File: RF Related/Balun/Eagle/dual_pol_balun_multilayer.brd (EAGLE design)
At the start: 54.6 x 48.6 mm, 8 parts, among them T1 ADT1-1WT+, T2 ADT1-1WT+, X1 SMA-142-0701-801/806, X2 SMA-142-0701-801/806, X3 SMA-142-0701-801/806, X4 SMA-142-0701-801/806, X5 SMA-142-0701-801/806, X6 SMA-142-0701-801/806

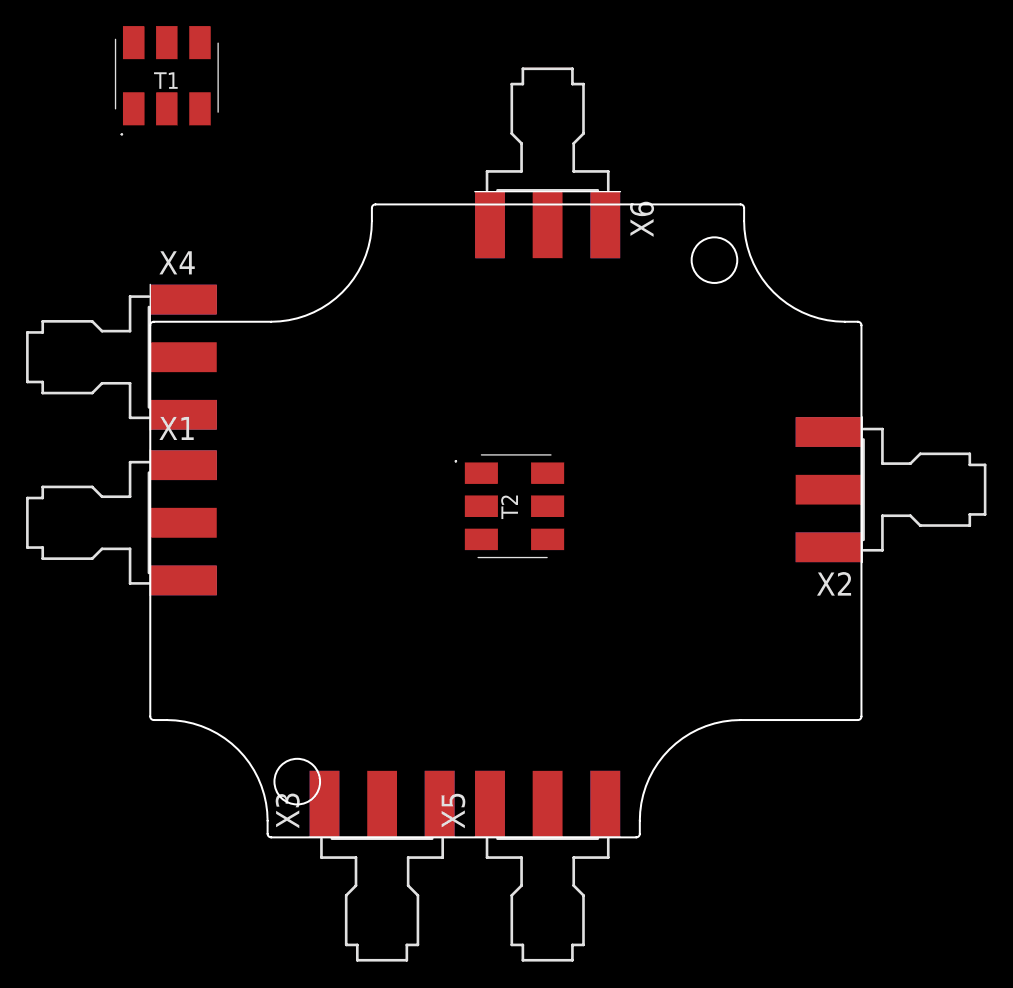
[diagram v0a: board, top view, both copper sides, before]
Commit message: also updated entire drone 3D model to contain primary balun candidate.
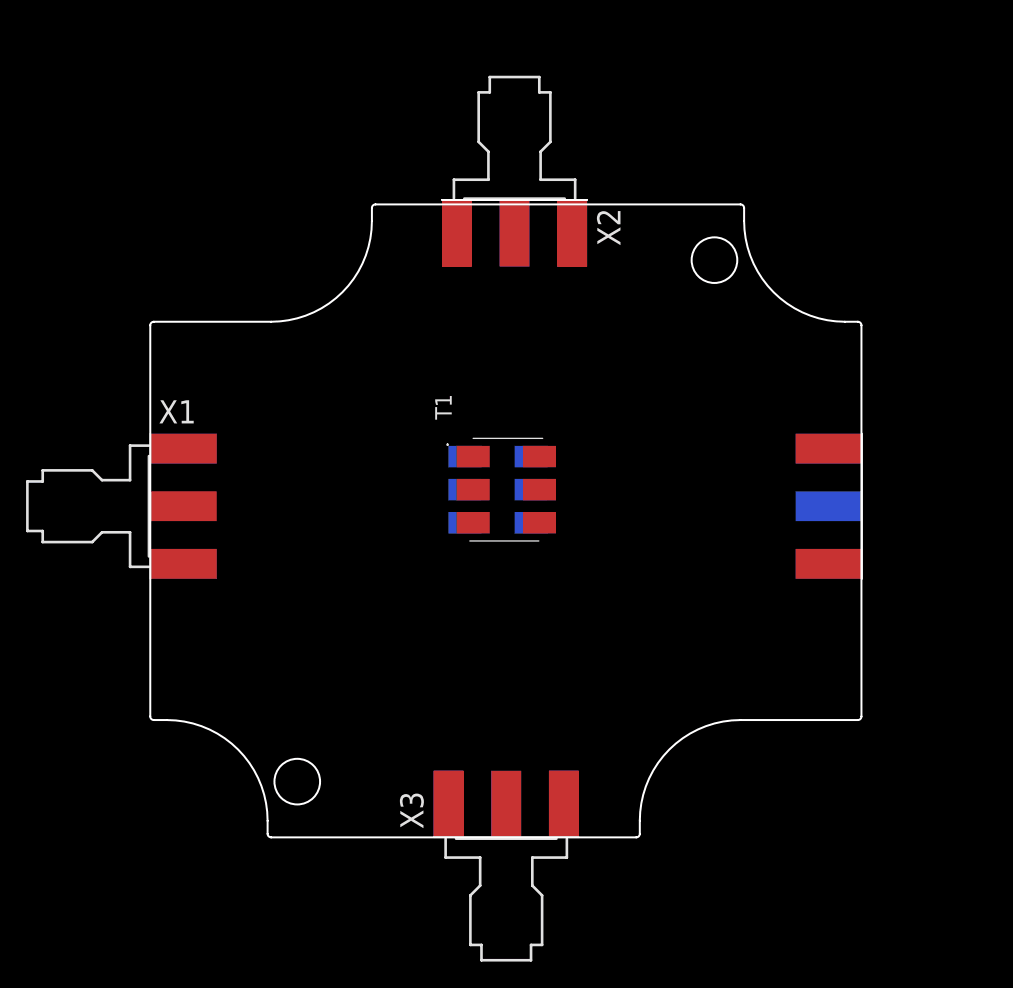
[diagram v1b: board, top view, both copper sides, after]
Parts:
- moved X4 55.8 mm to (54.6, 25.4), flipped to the bottom
- moved X6 49.6 mm to (27.3, 0.00), flipped to the bottom, turned to 90 degrees
- moved X5 49.0 mm to (27.9, 48.9), flipped to the bottom, turned to 270 degrees
- moved T1 41.1 mm to (27.3, 26.7), turned to 270 degrees
- moved X2 34.7 mm to (27.9, 48.9), turned to 270 degrees
- moved X3 9.52 mm to (27.3, 0.00)
- moved T2 1.80 mm to (26.7, 26.7), flipped to the bottom
- moved X1 1.27 mm to (0.00, 25.4)
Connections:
- net GND: now also T1.3, T2.3
